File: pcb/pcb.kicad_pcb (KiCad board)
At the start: 2 copper layers, 71.5 x 115.4 mm, 163 parts, among them J1 AudioJack3_SwitchTR, J100 Conn_02x05_Odd_Even, J102 Conn_01x03, J500 FPC_18P_1.0MM, J600 USB_B_Micro, Q300 IRLML6402, SW1 SW_SP3T, SW700 SW_Push, SW701 SW_Push, SW702 SW_Push, SW703 SW_Push, SW704 SW_Push, SW705 SW_Push, SW706 SW_Push, SW707 SW_Push, U1 LTC3456, U100 LPC5500, U300 TXS0108EPW, U400 CS43130, U401 ADP150-3.0, U402 ADP150-1.8, U403 ADP150-1.8, U500 LT1615, U501 LT1617, U502 LM324, U503 TXS0108EPW, U600 USBLC6-2SC6, X1 DSC1001CE2-022.5792, Y1 32.768kHz, Y2 24MHz

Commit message: pcb: fixing i2c numbering; add filtering for lcd
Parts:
- removed C303, C304: 100nF, Capacitor_SMD:C_0402_1005Metric
- removed C500, C501: 10uF, Capacitor_SMD:C_0603_1608Metric
- removed D500: MBR0530, Diode_SMD:D_SOD-123
- removed L502: 10uH, Inductor_SMD:L_Vishay_IHLP-1212
- removed U300, U503: TXS0108EPW, Package_SO:TSSOP-20_4.4x6.5mm_P0.65mm
- removed U500: LT1615, Package_TO_SOT_SMD:TSOT-23-5
- added C418: 100nF, Capacitor_SMD:C_0402_1005Metric, F.Cu at (214.6, 95.2)
- added C419: 100nF, Capacitor_SMD:C_0402_1005Metric, F.Cu at (218.6, 92.7)
- added C420: 100nF, Capacitor_SMD:C_0402_1005Metric, F.Cu at (217.5, 95.2)
- added C504: 4.7uF, Capacitor_SMD:C_0603_1608Metric, F.Cu at (225.8, 92.7)
- added C505: 4.7uF, Capacitor_SMD:C_0603_1608Metric, F.Cu at (231.4, 89.5)
- added C506: 4.7uF, Capacitor_SMD:C_0603_1608Metric, F.Cu at (225.8, 95.2)
- added C507: 4.7uF, Capacitor_SMD:C_0603_1608Metric, F.Cu at (229.8, 92.7)
- added C509: 22uF, Capacitor_SMD:C_1206_3216Metric, F.Cu at (226.6, 89.8)
- added R405: 10K, Resistor_SMD:R_0603_1608Metric, F.Cu at (206.2, 96.2)
- added R406: 10K, Resistor_SMD:R_0603_1608Metric, F.Cu at (215.2, 93.0)
- added R407: 200K, Resistor_SMD:R_0603_1608Metric, F.Cu at (210.2, 96.2)
- added R512: 33, Resistor_SMD:R_0603_1608Metric, F.Cu at (235.4, 89.5)
- added R513: 33, Resistor_SMD:R_0603_1608Metric, F.Cu at (229.8, 95.2)
- added R514: 33, Resistor_SMD:R_0603_1608Metric, F.Cu at (233.8, 92.0)
- added REF**: MountingHole_3.5mm, MountingHole:MountingHole_3.5mm, F.Cu at (128.3, 127.1)
- added U404: SN74AVC4T245PW, Package_SO:TSSOP-16_4.4x5mm_P0.65mm, F.Cu at (208.7, 91.6)
- added U405: PCA9306, Package_SO:VSSOP-8_2.3x2mm_P0.5mm, F.Cu at (215.9, 90.0)
- C502: value 100nF -> 4.7uF; footprint Capacitor_SMD:C_0402_1005Metric -> Capacitor_SMD:C_0603_1608Metric
- R510: value 91K -> 33
- R511: value 30K -> 33
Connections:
- C15 pad 1: +1V8 -> +3V3
- C16 pad 1: +1V8 -> +3V3
- C17 pad 1: +1V8 -> +3V3
- C502 pad 1: +1V8 -> GND
- C502 pad 2: GND -> /lcd/LCD_V5
- C503 pad 2: +5V -> +3V3
- C512 pad 2: /lcd/LCD_V5 -> Net-(C512-Pad2)
- D300 pad 2: /storage/SD_PWR_EN -> ~SD0_PWR_EN
- J1 pad RN: Net-(J1-PadRN) -> (no net)
- J1 pad TN: Net-(J1-PadTN) -> (no net)
- J100 pad 7: Net-(J100-Pad7) -> (no net)
- J100 pad 8: Net-(J100-Pad8) -> (no net)
- J100 pad 9: Net-(J100-Pad9) -> (no net)
- J500 pad 14: +5V -> +3V3
- J600 pad 4: Net-(J600-Pad4) -> (no net)
- L5 pad 1: +1V8 -> +3V3
- L501 pad 2: /lcd/LCD_V5 -> Net-(C512-Pad2)
- L6 pad 1: +1V8 -> +3V3
- MICRO_SD300 pad 1: /storage/SD_D2 -> SD0_D2
- MICRO_SD300 pad 2: /storage/SD_D3 -> SD0_D3
- MICRO_SD300 pad 3: /storage/SD_CMD -> SD0_CMD
- MICRO_SD300 pad 7: /storage/SD_D0 -> SD0_D0
- MICRO_SD300 pad 8: /storage/SD_D1 -> SD0_D1
- R110 pad 2: I2C1_SCL -> I2C1_SDA
- R111 pad 2: I2C1_SDA -> I2C1_SCL
- R302 pad 2: /storage/SD_CMD -> SD0_CMD
- R303 pad 2: /storage/SD_CLK -> SD0_CLK
- R401 pad 2: SAI1_TXD -> Net-(R401-Pad2)
- R402 pad 2: SAI1_TXFS -> Net-(R402-Pad2)
- R403 pad 2: SAI1_TXC -> Net-(R403-Pad2)
- R503 pad 2: /lcd/LCD_V5 -> Net-(C512-Pad2)
- R504 pad 2: /lcd/LCD_V5 -> Net-(C512-Pad2)
- R508 pad 1: +5V -> +3V3
- R510 pad 1: Net-(R510-Pad1) -> /lcd/LCD_V1
- R510 pad 2: +5V -> Net-(R510-Pad2)
- R511 pad 1: Net-(R510-Pad1) -> /lcd/LCD_V2
- R511 pad 2: GND -> Net-(R511-Pad2)
- RN502 pad 1: Net-(RN502-Pad1) -> STN_S
- RN502 pad 2: Net-(RN502-Pad2) -> STN_FR
- RN502 pad 3: Net-(RN502-Pad3) -> STN_CP
- RN502 pad 4: Net-(RN502-Pad4) -> STN_D1
- RN503 pad 1: Net-(RN503-Pad1) -> STN_D0
- RN503 pad 2: Net-(RN503-Pad2) -> STN_ST
- RN503 pad 3: Net-(RN503-Pad3) -> STN_CPL
- RN503 pad 4: Net-(RN503-Pad4) -> STN_CPG
- SW1 pad 2: Net-(SW1-Pad2) -> (no net)
- U1 pad 11: Net-(U1-Pad11) -> (no net)
- U1 pad 17: Net-(U1-Pad17) -> (no net)
- U1 pad 7: Net-(U1-Pad7) -> (no net)
- U1 pad 9: Net-(U1-Pad9) -> (no net)
- U100 pad 22: Net-(U100-Pad22) -> (no net)
- U100 pad 24: Net-(U100-Pad24) -> (no net)
- U100 pad 27: Net-(U100-Pad27) -> (no net)
- U100 pad 30: Net-(U100-Pad30) -> (no net)
- U100 pad 31: Net-(U100-Pad31) -> (no net)
- U100 pad 49: +1V8 -> +3V3
- U100 pad 50: +1V8 -> +3V3
- U100 pad 51: +1V8 -> +3V3
- U100 pad 54: Net-(U100-Pad54) -> (no net)
- U100 pad 56: Net-(U100-Pad56) -> (no net)
- U100 pad 57: Net-(U100-Pad57) -> (no net)
- U100 pad 59: Net-(U100-Pad59) -> (no net)
- U100 pad 71: I2C1_SCL -> I2C1_SDA
- U100 pad 72: I2C1_SDA -> I2C1_SCL
- U100 pad 73: Net-(U100-Pad73) -> (no net)
- U100 pad 77: Net-(U100-Pad77) -> (no net)
- U100 pad 78: Net-(U100-Pad78) -> (no net)
- U100 pad 80: Net-(U100-Pad80) -> (no net)
- U100 pad 81: Net-(U100-Pad81) -> (no net)
- U100 pad 82: Net-(U100-Pad82) -> (no net)
- U100 pad 83: Net-(U100-Pad83) -> (no net)
- U100 pad 85: Net-(U100-Pad85) -> (no net)
- U100 pad 86: Net-(U100-Pad86) -> (no net)
- U100 pad 88: Net-(U100-Pad88) -> (no net)
- U100 pad 89: Net-(U100-Pad89) -> (no net)
- U100 pad 97: Net-(U100-Pad97) -> (no net)
- U100 pad 98: Net-(U100-Pad98) -> (no net)
- U400 pad 1: I2C1_SCL -> Net-(R406-Pad1)
- U400 pad 22: Net-(J1-PadTN) -> (no net)
- U400 pad 28: POR -> Net-(U400-Pad28)
- U400 pad 29: Net-(U400-Pad29) -> (no net)
- U400 pad 32: Net-(U400-Pad32) -> (no net)
- U400 pad 36: Net-(U400-Pad36) -> (no net)
- U400 pad 39: I2C1_SDA -> Net-(R405-Pad1)
- U400 pad 40: Net-(U400-Pad40) -> (no net)
- U401 pad 4: Net-(U401-Pad4) -> (no net)
- U402 pad 4: Net-(U402-Pad4) -> (no net)
- U403 pad 4: Net-(U403-Pad4) -> (no net)
- U502 pad 1: /lcd/LCD_V1 -> Net-(R510-Pad2)
- U502 pad 11: /lcd/LCD_V5 -> Net-(C512-Pad2)
- U502 pad 13: /lcd/LCD_V4 -> Net-(R513-Pad2)
- U502 pad 14: /lcd/LCD_V4 -> Net-(R513-Pad2)
- U502 pad 2: /lcd/LCD_V1 -> Net-(R510-Pad2)
- U502 pad 4: +5V -> +3V3
- U502 pad 6: /lcd/LCD_V2 -> Net-(R511-Pad2)
- U502 pad 7: /lcd/LCD_V2 -> Net-(R511-Pad2)
- U502 pad 8: /lcd/LCD_V3 -> Net-(R512-Pad2)
- U502 pad 9: /lcd/LCD_V3 -> Net-(R512-Pad2)
- U600 pad 5: Net-(U600-Pad5) -> (no net)
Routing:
- net GND: track 129.2 -> 104.9 mm, vias 195 -> 185
- net SD0_D2: track 12.8 -> 35.1 mm
- net /storage/SD_D2: track 22.4 -> 0.00 mm
- net SD0_D3: track 19.5 -> 39.2 mm
- net /storage/SD_D3: track 19.7 -> 0.00 mm
- net SD0_CMD: track 11.5 -> 29.4 mm
- net /storage/SD_CMD: track 17.9 -> 0.00 mm
- net SD0_D0: track 35.1 -> 47.8 mm
- net /storage/SD_D0: track 12.7 -> 0.00 mm
- net SD0_D1: track 39.1 -> 49.3 mm
- net /storage/SD_D1: track 10.3 -> 0.00 mm
- net /storage/SD_PWR_EN: track 9.65 -> 0.00 mm
- net ~SD0_PWR_EN: track 25.3 -> 35.0 mm
- net STN_S: track 6.81 -> 15.8 mm
- net Net-(RN502-Pad1): track 8.95 -> 0.00 mm
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- added copper zone on In1.Cu, net +3V3
- added copper zone on In1.Cu, net GND
- added copper zone on In2.Cu, net GND
- added copper zone on In1.Cu, net Net-(C20-Pad1)
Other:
- copper layers 2 -> 4

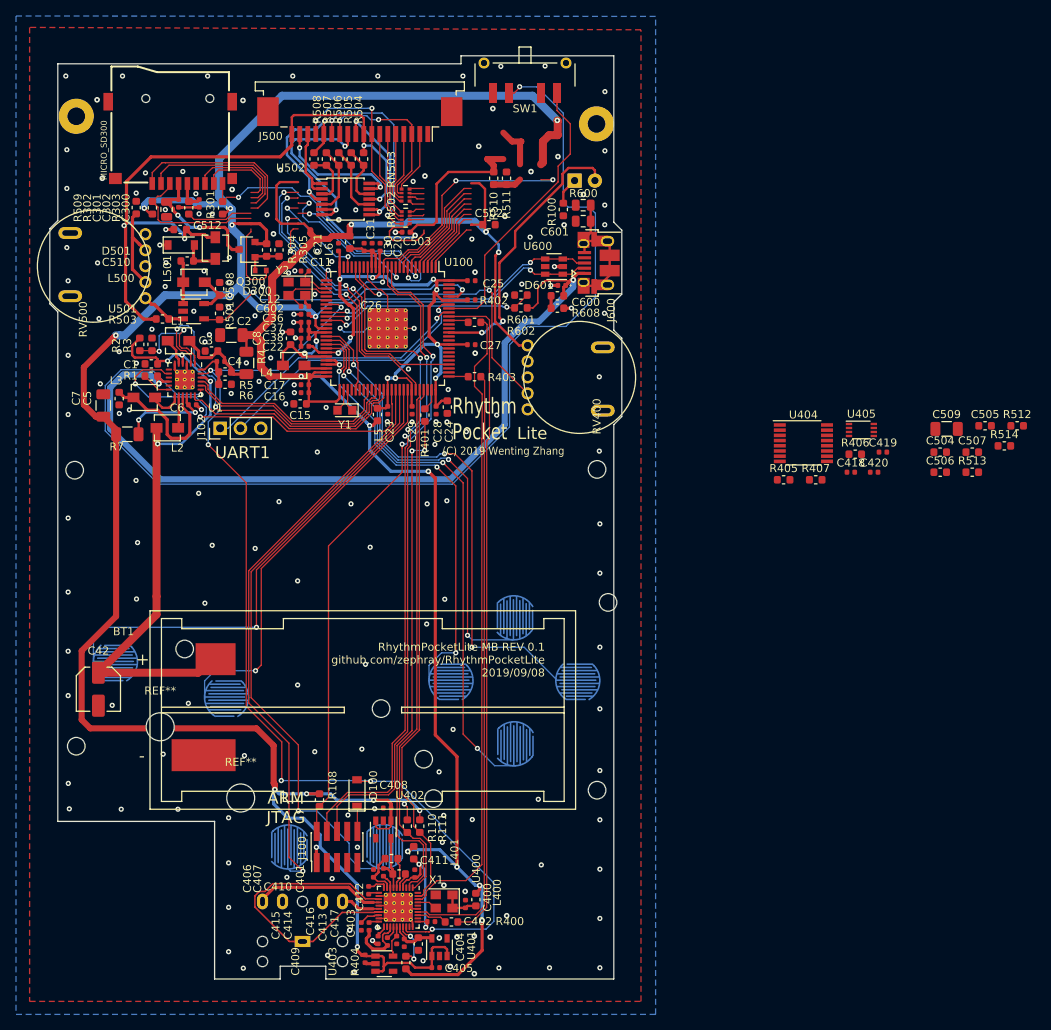
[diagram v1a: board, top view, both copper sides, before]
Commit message: pcb: use crystal instead
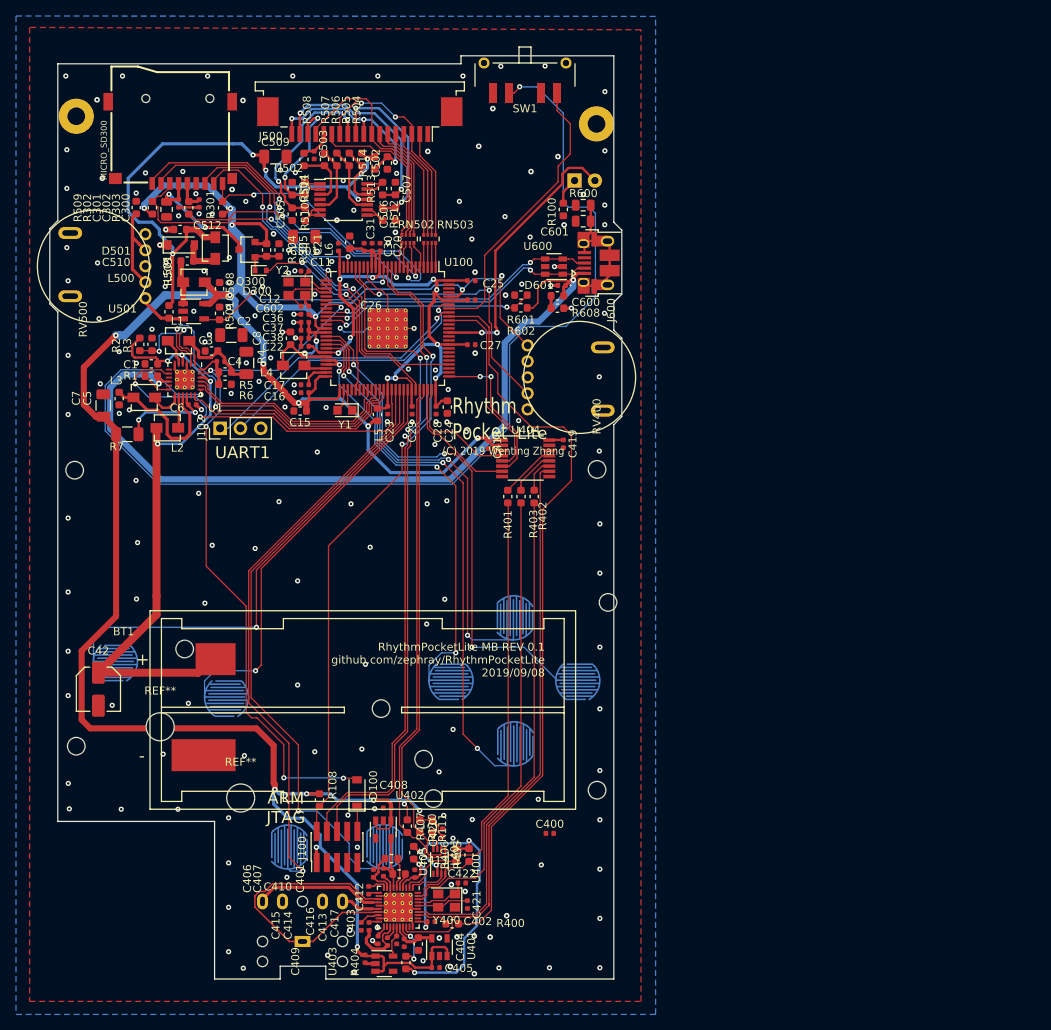
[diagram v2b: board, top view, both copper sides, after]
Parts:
- removed L400: 120R, Inductor_SMD:L_0603_1608Metric
- removed X1: DSC1001CE2-022.5792, Oscillator:Oscillator_SMD_Abracon_ASE-4Pin_3.2x2.5mm
- added C421: 18pF, Capacitor_SMD:C_0402_1005Metric, F.Cu at (166.7, 149.3)
- added C422: 18pF, Capacitor_SMD:C_0402_1005Metric, F.Cu at (166.0, 146.6)
- added C501: 22uF/25V, Capacitor_SMD:C_1206_3216Metric, F.Cu at (146.3, 65.8)
- added Y400: 22.5792MHz, Oscillator:Oscillator_SMD_Abracon_ASE-4Pin_3.2x2.5mm, F.Cu at (164.1, 148.8)
- C400: value 100nF -> 10uF
- C509: value 22uF -> 22uF/25V
- C512: value 10uF -> 4.7uF/25V
- moved C505 90.6 mm to (144.8, 63.0), turned to 90 degrees
- moved C509 90.5 mm to (142.7, 55.8)
- moved C504 87.4 mm to (144.8, 59.8), turned to 270 degrees
- moved R514 86.3 mm to (155.1, 56.6), turned to 90 degrees
- moved R512 83.6 mm to (156.1, 63.0), turned to 270 degrees
- moved R513 81.8 mm to (156.1, 59.8), turned to 90 degrees
- moved C507 79.3 mm to (157.7, 59.8), turned to 270 degrees
- moved U405 75.4 mm to (163.2, 143.9), turned to 90 degrees
- moved C506 75.4 mm to (157.7, 63.0), turned to 90 degrees
- moved R406 70.7 mm to (165.3, 143.1), turned to 90 degrees
- moved C420 70.3 mm to (163.6, 140.3), turned to 90 degrees
- moved R407 64.6 mm to (162.3, 139.5), turned to 90 degrees
- moved R405 61.2 mm to (166.9, 143.1), turned to 90 degrees
- moved C418 45.5 mm to (169.3, 91.8), turned to 270 degrees
- moved C419 40.0 mm to (178.7, 91.7), turned to 270 degrees
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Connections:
- C401 pad 1: Net-(C401-Pad1) -> Net-(C400-Pad1)
- C402 pad 1: Net-(C401-Pad1) -> Net-(C400-Pad1)
- C405 pad 1: +3V3 -> Net-(C405-Pad1)
- C408 pad 1: +3V3 -> Net-(C405-Pad1)
- C409 pad 1: +3V3 -> Net-(C405-Pad1)
- C509 pad 1: (no net) -> Net-(C501-Pad1)
- C509 pad 2: (no net) -> GND
- C512 pad 2: Net-(C512-Pad2) -> Net-(C501-Pad1)
- J1 pad RN: (no net) -> Net-(J1-PadRN)
- J1 pad TN: (no net) -> Net-(J1-PadTN)
- J100 pad 7: (no net) -> Net-(J100-Pad7)
- J100 pad 8: (no net) -> Net-(J100-Pad8)
- J100 pad 9: (no net) -> Net-(J100-Pad9)
- J600 pad 4: (no net) -> Net-(J600-Pad4)
- L401 pad 2: Net-(C401-Pad1) -> Net-(C400-Pad1)
- L501 pad 2: Net-(C512-Pad2) -> Net-(C501-Pad1)
- R503 pad 2: Net-(C512-Pad2) -> Net-(C501-Pad1)
- R504 pad 2: Net-(C512-Pad2) -> Net-(C501-Pad1)
- R514 pad 2: Net-(C512-Pad2) -> Net-(C501-Pad1)
- REF** pad : (no net) -> +3V3
- RV400 pad 1: +1V8 -> +3V3
- SW1 pad 2: (no net) -> Net-(SW1-Pad2)
- U1 pad 11: (no net) -> Net-(U1-Pad11)
- U1 pad 17: (no net) -> Net-(U1-Pad17)
- U1 pad 7: (no net) -> Net-(U1-Pad7)
- U1 pad 9: (no net) -> Net-(U1-Pad9)
- U100 pad 1: STN_S -> STN_CPG
- U100 pad 10: STN_CPG -> STN_S
- U100 pad 2: STN_FR -> STN_CPL
- U100 pad 22: (no net) -> Net-(U100-Pad22)
- U100 pad 24: (no net) -> Net-(U100-Pad24)
- U100 pad 27: (no net) -> Net-(U100-Pad27)
- U100 pad 3: STN_CP -> STN_ST
- U100 pad 30: (no net) -> Net-(U100-Pad30)
- U100 pad 31: (no net) -> Net-(U100-Pad31)
- U100 pad 4: STN_D1 -> STN_D0
- U100 pad 5: STN_D0 -> STN_D1
- U100 pad 54: (no net) -> Net-(U100-Pad54)
- U100 pad 56: (no net) -> Net-(U100-Pad56)
- U100 pad 57: (no net) -> Net-(U100-Pad57)
- U100 pad 59: (no net) -> Net-(U100-Pad59)
- U100 pad 7: STN_ST -> STN_CP
- U100 pad 73: (no net) -> CODEC_RST
- U100 pad 77: (no net) -> Net-(U100-Pad77)
- U100 pad 78: (no net) -> Net-(U100-Pad78)
- U100 pad 80: (no net) -> Net-(U100-Pad80)
- U100 pad 81: (no net) -> Net-(U100-Pad81)
- U100 pad 82: (no net) -> Net-(U100-Pad82)
- U100 pad 83: (no net) -> Net-(U100-Pad83)
- U100 pad 85: (no net) -> Net-(U100-Pad85)
- U100 pad 86: (no net) -> Net-(U100-Pad86)
- U100 pad 88: (no net) -> Net-(U100-Pad88)
- U100 pad 89: (no net) -> Net-(U100-Pad89)
- U100 pad 9: STN_CPL -> STN_FR
- U100 pad 97: (no net) -> Net-(U100-Pad97)
- U100 pad 98: (no net) -> Net-(U100-Pad98)
- U400 pad 22: (no net) -> Net-(U400-Pad22)
- U400 pad 29: (no net) -> Net-(U400-Pad29)
- U400 pad 31: Net-(C401-Pad1) -> Net-(C400-Pad1)
- U400 pad 32: (no net) -> Net-(U400-Pad32)
- U400 pad 36: (no net) -> Net-(C421-Pad1)
- U400 pad 4: Net-(C401-Pad1) -> Net-(C400-Pad1)
- U400 pad 40: (no net) -> Net-(U400-Pad40)
- U401 pad 1: +3V3 -> Net-(C405-Pad1)
- U401 pad 3: +3V3 -> Net-(C405-Pad1)
- U401 pad 4: (no net) -> Net-(U401-Pad4)
- U402 pad 1: +3V3 -> Net-(C405-Pad1)
- U402 pad 3: +3V3 -> Net-(C405-Pad1)
- U402 pad 4: (no net) -> Net-(U402-Pad4)
- U403 pad 1: +3V3 -> Net-(C405-Pad1)
- U403 pad 3: +3V3 -> Net-(C405-Pad1)
- U403 pad 4: (no net) -> Net-(U403-Pad4)
- U404 pad 7: (no net) -> CODEC_RST
- U502 pad 11: Net-(C512-Pad2) -> Net-(C501-Pad1)
- U600 pad 5: (no net) -> Net-(U600-Pad5)
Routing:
- net +1V8: track 214.9 -> 40.8 mm, vias 10 -> 4
- net Net-(U400-Pad28): track 0.00 -> 71.1 mm
- net Net-(C501-Pad1): track 0.00 -> 70.6 mm, vias 0 -> 5
- net /lcd/LCD_V5: track 83.7 -> 25.0 mm, vias 4 -> 3
- net +5V: track 57.5 -> 0.00 mm, vias 3 -> 0
- net POR: track 130.1 -> 88.8 mm, vias 6 -> 5
- net +3V3: track 321.5 -> 359.5 mm, vias 15 -> 19
- net ~LCD_PWR_EN: track 56.9 -> 27.0 mm, vias 4 -> 2
- net SAI1_TXFS: track 2.51 -> 24.2 mm
- net Net-(R402-Pad1): track 79.5 -> 58.0 mm
- net SAI1_TXC: track 2.42 -> 19.2 mm, vias 0 -> 2
- net CODEC_RST: track 0.00 -> 16.4 mm
- net Net-(C401-Pad1): track 15.8 -> 0.00 mm, vias 2 -> 0
- net STN_CPG: track 16.6 -> 3.03 mm
- net Net-(R403-Pad1): track 75.3 -> 61.9 mm
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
